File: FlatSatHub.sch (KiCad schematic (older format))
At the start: 0 parts

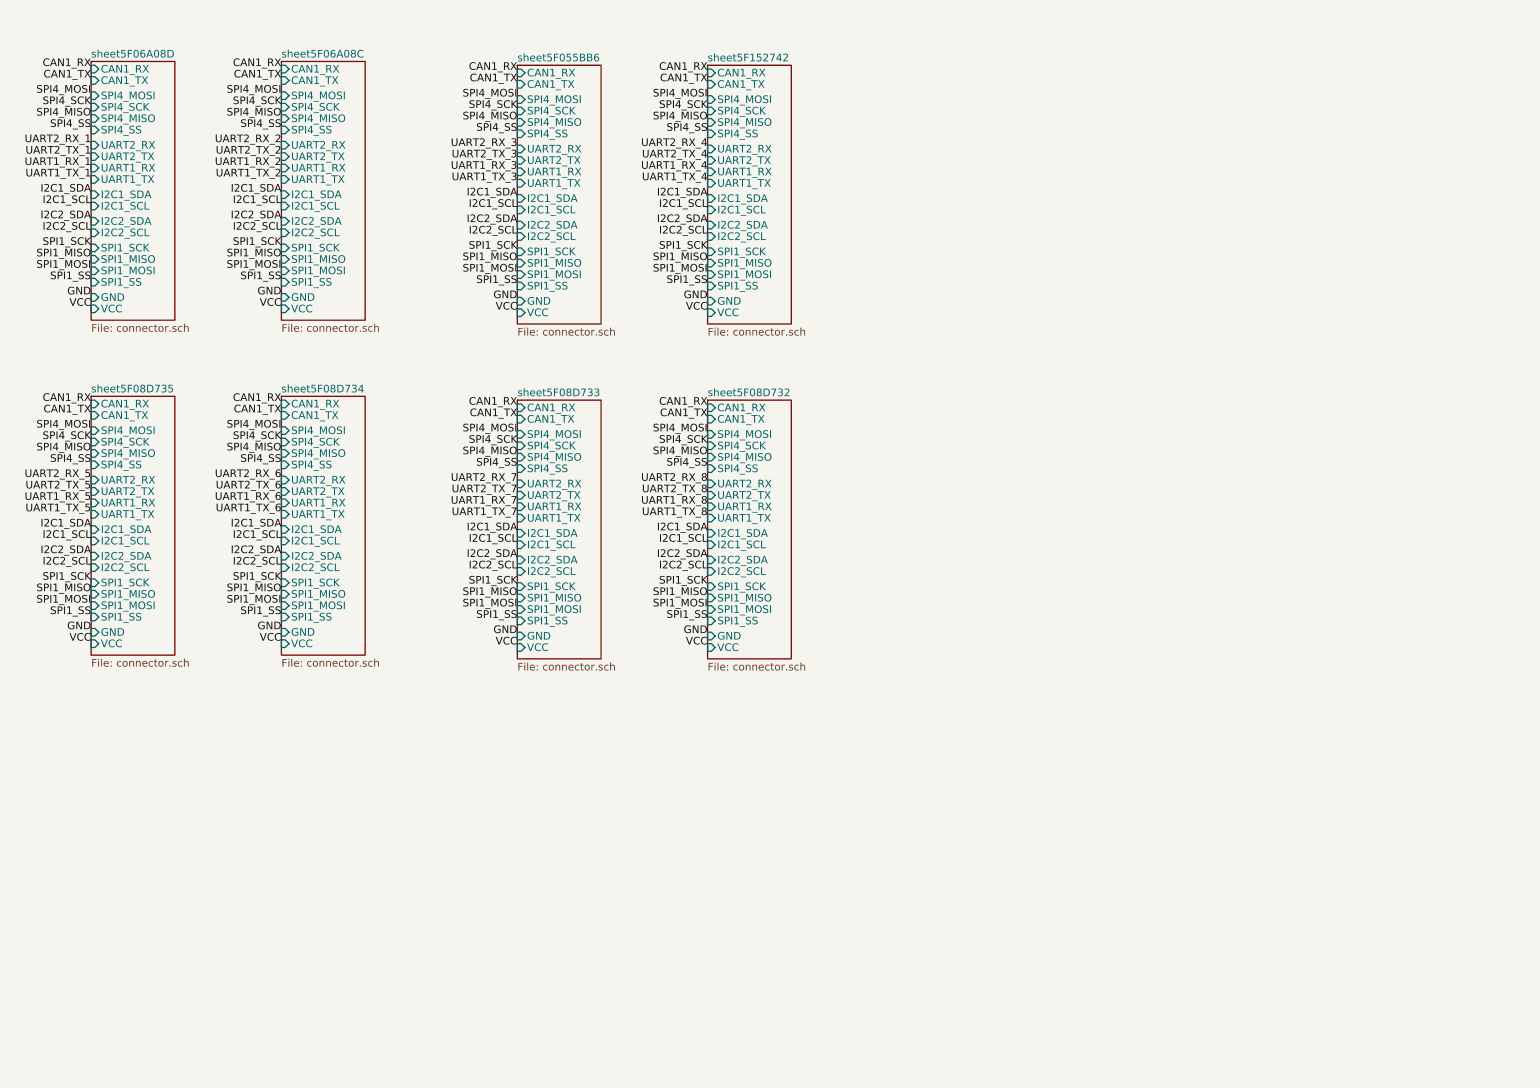
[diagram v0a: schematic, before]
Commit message: create cutout
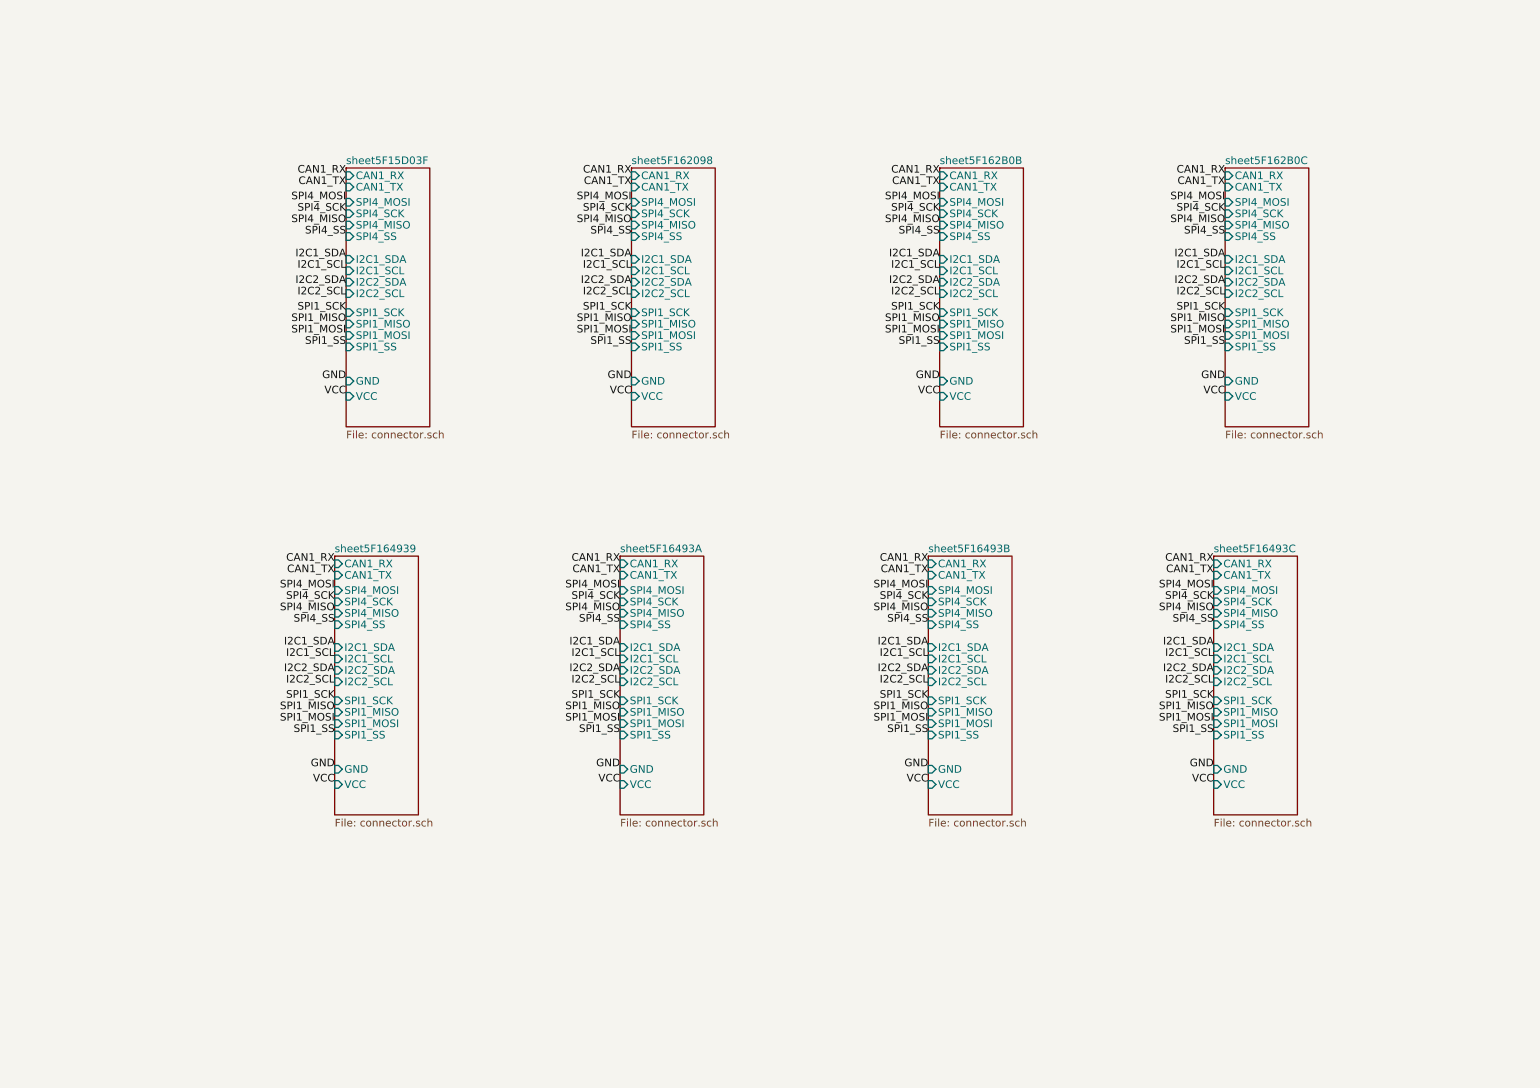
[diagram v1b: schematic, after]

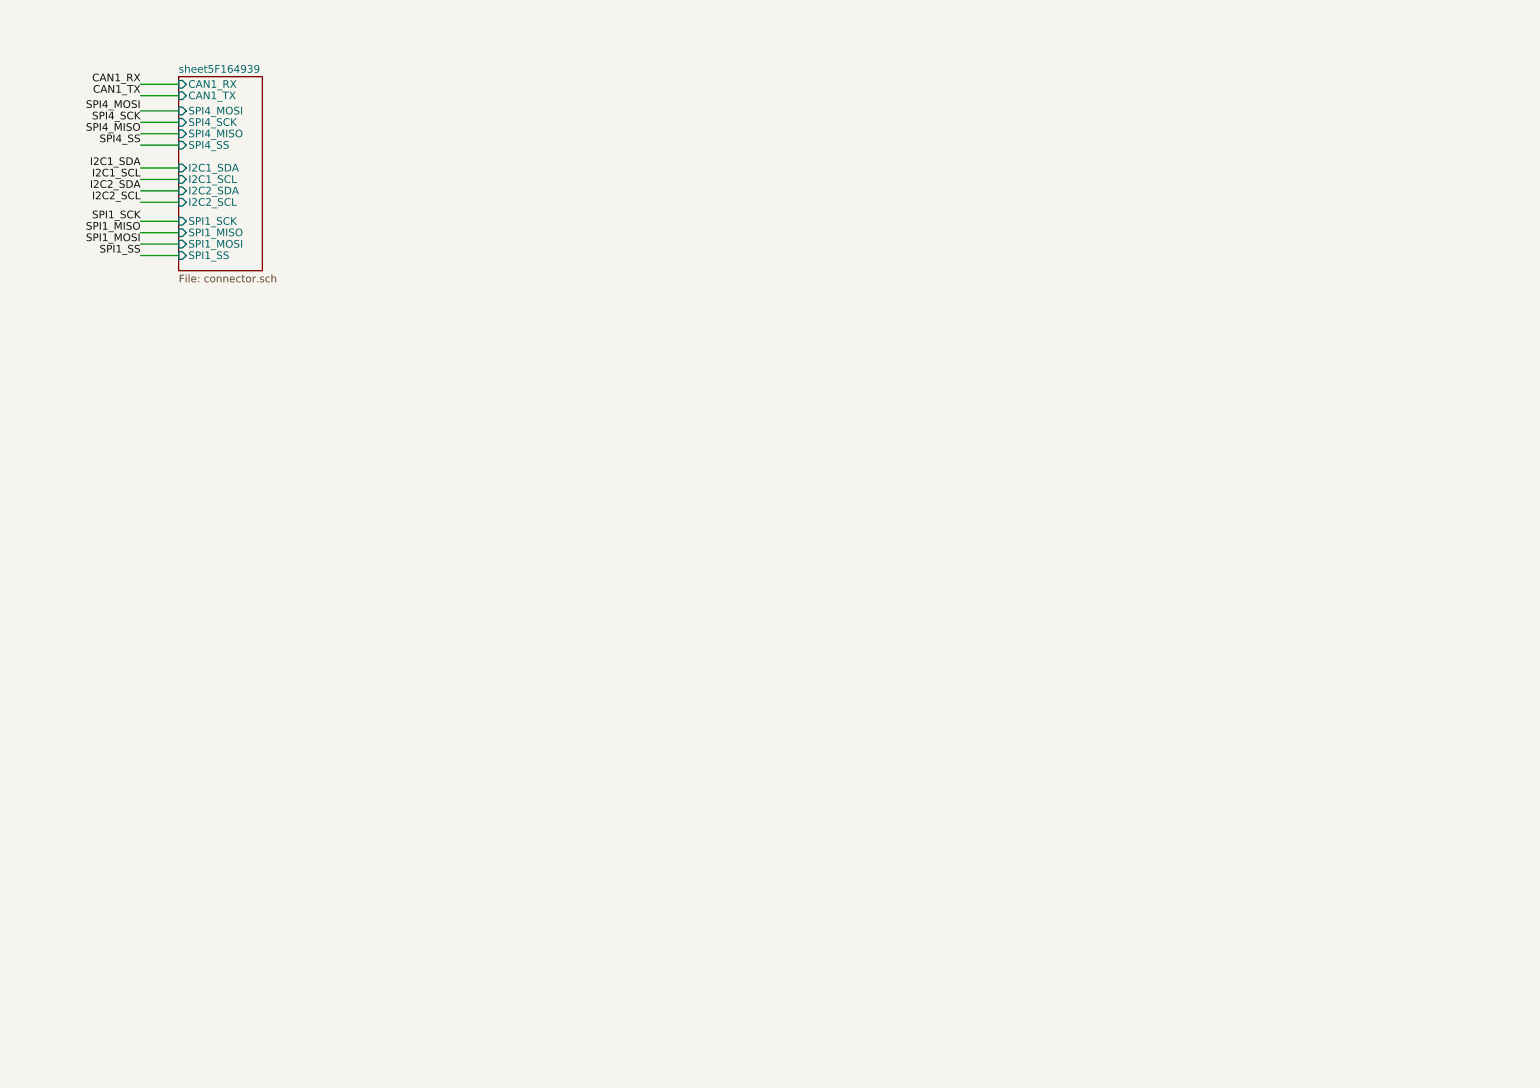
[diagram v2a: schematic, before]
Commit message: add power management wiring and mounting holes
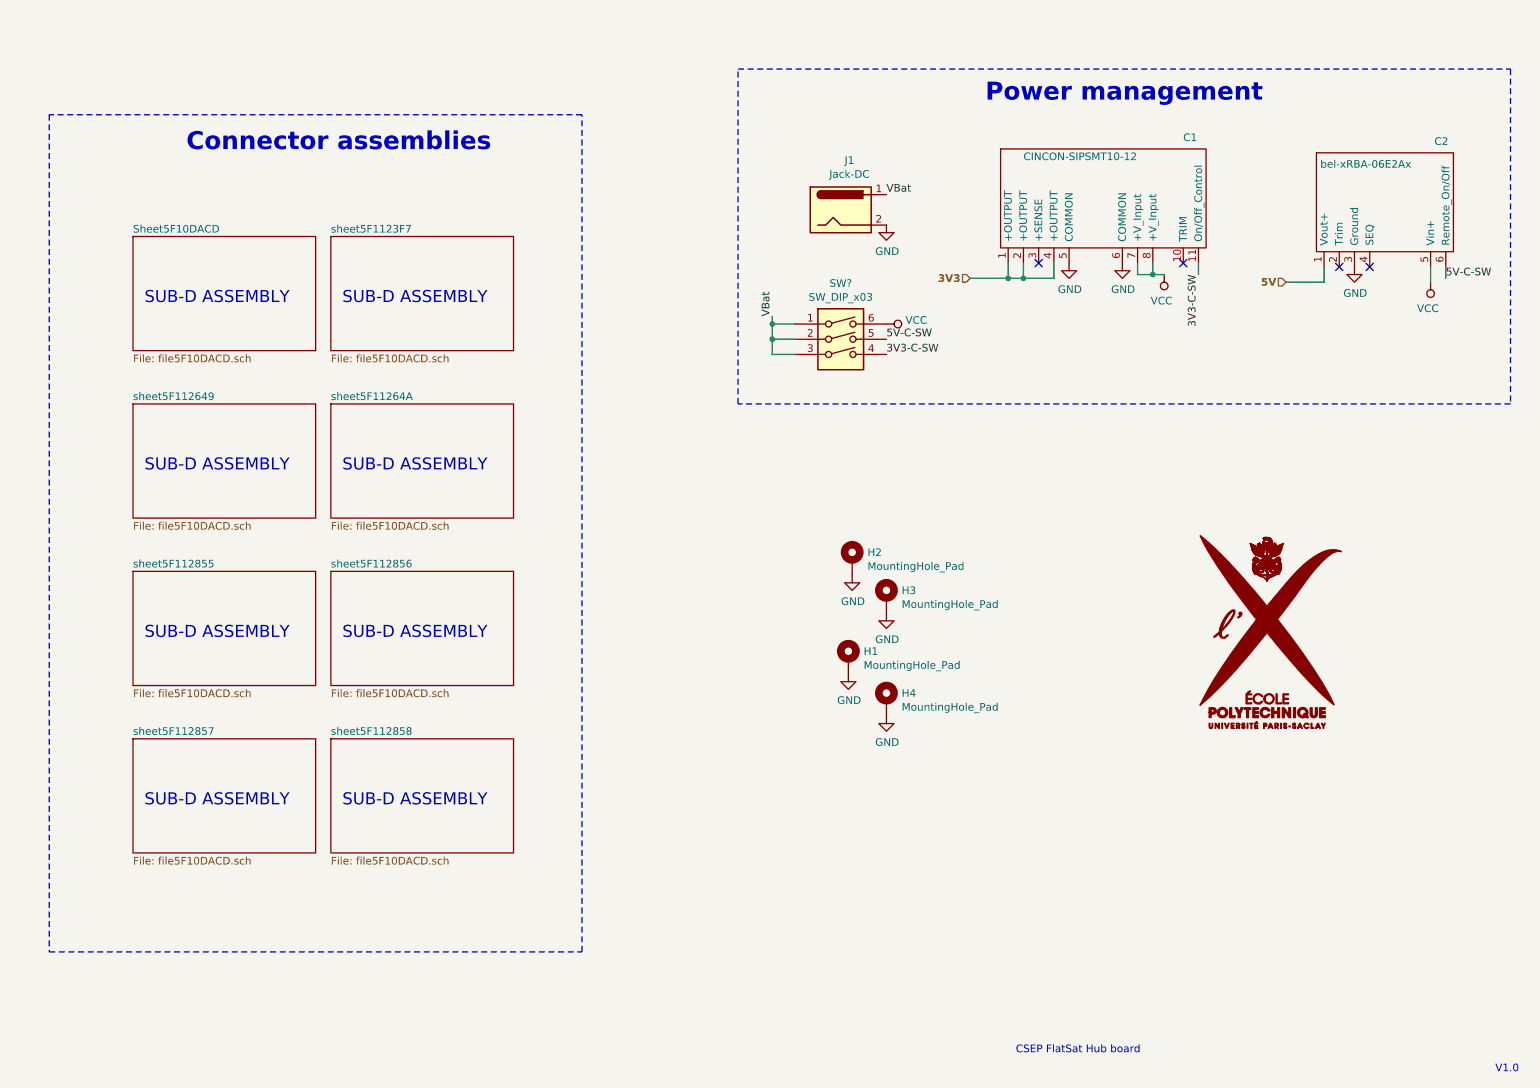
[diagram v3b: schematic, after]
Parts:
- added C1: CINCON-SIPSMT10-12, symbol FlatSatHub:CINCON-SIPSMT10-12
- added C2: bel-xRBA-06E2Ax, symbol FlatSatHub:bel-xRBA-06E2Ax
- added H1, H2, H3, H4: MountingHole_Pad, symbol Mechanical:MountingHole_Pad
- added J1: Jack-DC, symbol Connector:Jack-DC
- added SW?: SW_DIP_x03, symbol Switch:SW_DIP_x03
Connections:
- new net 3V3: C1.1 (+OUTPUT), C1.2 (+OUTPUT), C1.4 (+OUTPUT)
- new net 3V3-C-SW: C1.11 (On/Off_Control), SW?.4
- new net 5V: C2.1 (Vout+)
- new net 5V-C-SW: C2.6 (Remote_On/Off), SW?.5
- new net GND: C1.5 (COMMON), C1.6 (COMMON), C2.3 (Ground), H1.1, H2.1, H3.1, H4.1, J1.2
- new net VBat: J1.1, SW?.1, SW?.2, SW?.3
- new net VCC: C1.7 (+V_Input), C1.8 (+V_Input), C2.5 (Vin+), SW?.6
- no-connect marks 0 -> 4
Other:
- note added: "CSEP FlatSat Hub board"
- note added: "Connector assemblies"
- note added: "Power management"
- note added: "SUB-D ASSEMBLY"
- note added: "V1.0"

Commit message: create footprints
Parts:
- C1: footprint (none) -> FlatSatHub:CINCON-SIPSMT10-12
- C2: footprint (none) -> FlatSatHub:BEL-xRBA-06E2Ax
- H1, H2, H3, H4: footprint (none) -> MountingHole:MountingHole_2.2mm_M2
- J1: footprint (none) -> Connector_BarrelJack:BarrelJack_CUI_PJ-063AH_Horizontal
- SW1: renamed from SW?; footprint (none) -> Button_Switch_THT:SW_DIP_SPSTx03_Slide_9.78x9.8mm_W7.62mm_P2.54mm
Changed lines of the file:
@@
 F 0 "J1" H 6332 2275 50  0000 C CNN
 F 1 "Jack-DC" H 6332 2184 50  0000 C CNN
-F 2 "" H 6325 1910 50  0001 C CNN
+F 2 "Connector_BarrelJack:BarrelJack_CUI_PJ-063AH_Horizontal" H 6325 1910 50  0001 C CNN
 F 3 "~" H 6325 1910 50  0001 C CNN
 	1    6275 1950
@@
 F 0 "C2" H 10175 2450 50  0000 L CNN
 F 1 "bel-xRBA-06E2Ax" H 9425 2300 50  0000 L CNN
-F 2 "" H 10150 2175 50  0001 C CNN
+F 2 "FlatSatHub:BEL-xRBA-06E2Ax" H 10150 2175 50  0001 C CNN
 F 3 "" H 10150 2175 50  0001 C CNN
 	1    9850 1975
@@
 F 0 "C1" H 8525 2525 50  0000 L CNN
 F 1 "CINCON-SIPSMT10-12" H 7475 2400 50  0000 L CNN
-F 2 "" H 8525 2150 50  0001 C CNN
+F 2 "FlatSatHub:CINCON-SIPSMT10-12" H 8525 2150 50  0001 C CNN
 F 3 "" H 8525 2150 50  0001 C CNN
 	1    7975 2000
@@
 F 0 "H2" H 6450 4299 50  0000 L CNN
 F 1 "MountingHole_Pad" H 6450 4208 50  0000 L CNN
-F 2 "" H 6350 4250 50  0001 C CNN
+F 2 "MountingHole:MountingHole_2.2mm_M2" H 6350 4250 50  0001 C CNN
 F 3 "~" H 6350 4250 50  0001 C CNN
 	1    6350 4250
@@
 F 0 "H3" H 6675 4549 50  0000 L CNN
 F 1 "MountingHole_Pad" H 6675 4458 50  0000 L CNN
-F 2 "" H 6575 4500 50  0001 C CNN
+F 2 "MountingHole:MountingHole_2.2mm_M2" H 6575 4500 50  0001 C CNN
 F 3 "~" H 6575 4500 50  0001 C CNN
 	1    6575 4500
@@
 F 0 "H1" H 6425 4949 50  0000 L CNN
 F 1 "MountingHole_Pad" H 6425 4858 50  0000 L CNN
-F 2 "" H 6325 4900 50  0001 C CNN
+F 2 "MountingHole:MountingHole_2.2mm_M2" H 6325 4900 50  0001 C CNN
 F 3 "~" H 6325 4900 50  0001 C CNN
 	1    6325 4900
@@
 F 0 "H4" H 6675 5224 50  0000 L CNN
 F 1 "MountingHole_Pad" H 6675 5133 50  0000 L CNN
-F 2 "" H 6575 5175 50  0001 C CNN
+F 2 "MountingHole:MountingHole_2.2mm_M2" H 6575 5175 50  0001 C CNN
 F 3 "~" H 6575 5175 50  0001 C CNN
 	1    6575 5175
@@
 $EndComp
 $Comp
-L Switch:SW_DIP_x03 SW?
+L Switch:SW_DIP_x03 SW1
 U 1 1 5F17DC40
 P 6275 2900
-F 0 "SW?" H 6275 3367 50  0000 C CNN
+F 0 "SW1" H 6275 3367 50  0000 C CNN
 F 1 "SW_DIP_x03" H 6275 3276 50  0000 C CNN
-F 2 "" H 6275 2900 50  0001 C CNN
+F 2 "Button_Switch_THT:SW_DIP_SPSTx03_Slide_9.78x9.8mm_W7.62mm_P2.54mm" H 6275 2900 50  0001 C CNN
 F 3 "~" H 6275 2900 50  0001 C CNN
 	1    6275 2900
@@
 VBat
 $Comp
-L power:VCC #PWR?
+L power:VCC #PWR0101
 U 1 1 5F1868C5
 P 6575 2700
-F 0 "#PWR?" H 6575 2550 50  0001 C CNN
+F 0 "#PWR0101" H 6575 2550 50  0001 C CNN
 F 1 "VCC" V 6550 2825 50  0000 L CNN
 F 2 "" H 6575 2700 50  0001 C CNN

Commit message: First placement and autorouting
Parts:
- H1, H2, H3, H4: footprint MountingHole:MountingHole_2.2mm_M2 -> MountingHole:MountingHole_2.2mm_M2_Pad
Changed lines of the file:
@@
 F 0 "H2" H 6450 4299 50  0000 L CNN
 F 1 "MountingHole_Pad" H 6450 4208 50  0000 L CNN
-F 2 "MountingHole:MountingHole_2.2mm_M2" H 6350 4250 50  0001 C CNN
+F 2 "MountingHole:MountingHole_2.2mm_M2_Pad" H 6350 4250 50  0001 C CNN
 F 3 "~" H 6350 4250 50  0001 C CNN
 	1    6350 4250
@@
 F 0 "H3" H 6675 4549 50  0000 L CNN
 F 1 "MountingHole_Pad" H 6675 4458 50  0000 L CNN
-F 2 "MountingHole:MountingHole_2.2mm_M2" H 6575 4500 50  0001 C CNN
+F 2 "MountingHole:MountingHole_2.2mm_M2_Pad" H 6575 4500 50  0001 C CNN
 F 3 "~" H 6575 4500 50  0001 C CNN
 	1    6575 4500
@@
 F 0 "H1" H 6425 4949 50  0000 L CNN
 F 1 "MountingHole_Pad" H 6425 4858 50  0000 L CNN
-F 2 "MountingHole:MountingHole_2.2mm_M2" H 6325 4900 50  0001 C CNN
+F 2 "MountingHole:MountingHole_2.2mm_M2_Pad" H 6325 4900 50  0001 C CNN
 F 3 "~" H 6325 4900 50  0001 C CNN
 	1    6325 4900
@@
 F 0 "H4" H 6675 5224 50  0000 L CNN
 F 1 "MountingHole_Pad" H 6675 5133 50  0000 L CNN
-F 2 "MountingHole:MountingHole_2.2mm_M2" H 6575 5175 50  0001 C CNN
+F 2 "MountingHole:MountingHole_2.2mm_M2_Pad" H 6575 5175 50  0001 C CNN
 F 3 "~" H 6575 5175 50  0001 C CNN
 	1    6575 5175
